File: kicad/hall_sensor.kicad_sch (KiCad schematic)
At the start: 5 parts

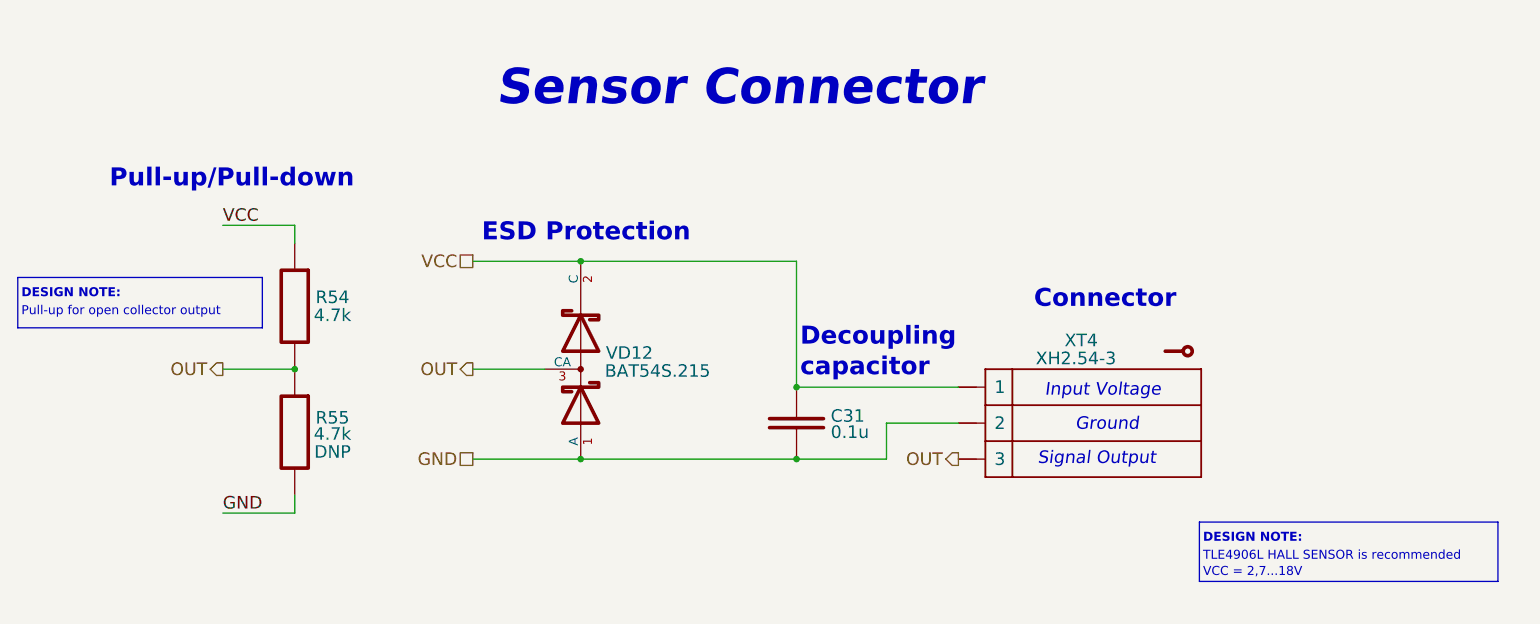
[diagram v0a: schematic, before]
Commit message: Reannotate schematic; Fix 5032 crystal footprint field; Update PCB with 5032 crystal
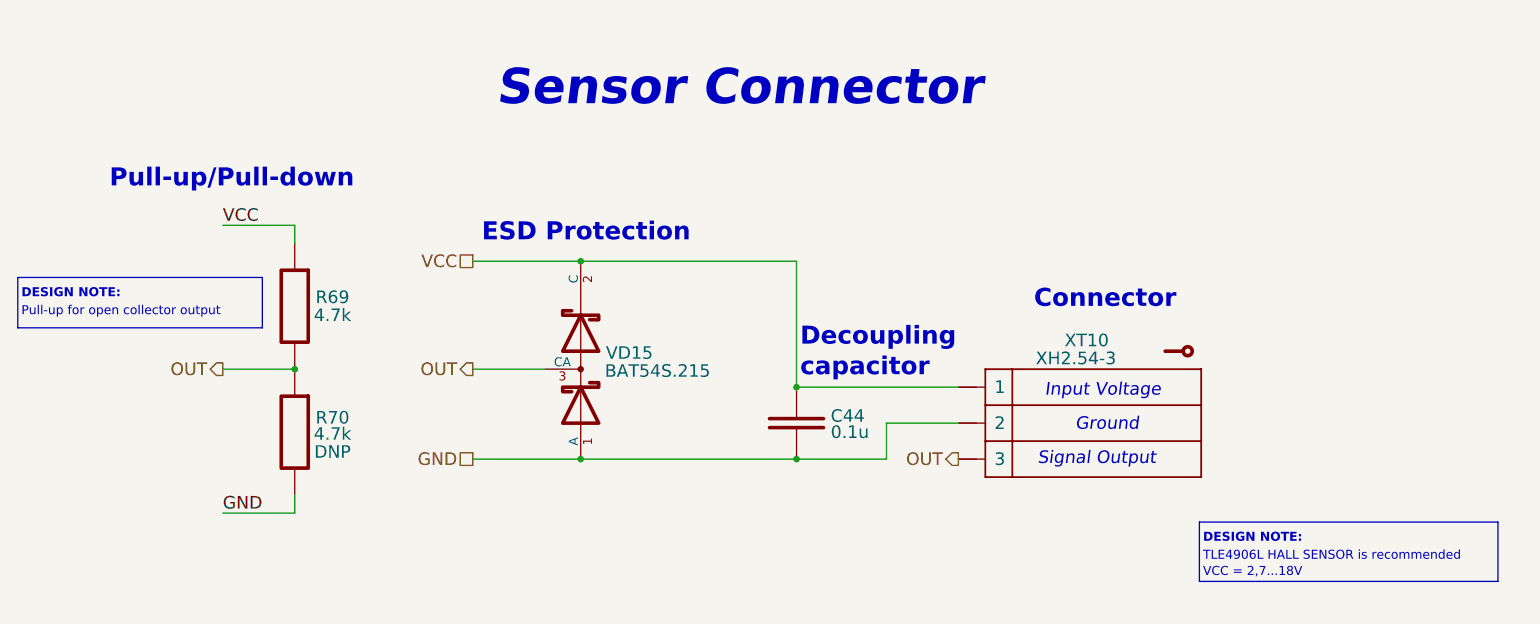
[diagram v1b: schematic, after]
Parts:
- renumbered C31 to C44, R54 to R69, R55 to R70, VD12 to VD15, XT4 to XT10
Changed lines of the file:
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@@
   (symbol (lib_id "Resistors:R_RES") (at 90.424 91.694 270) (unit 1)
     (in_bom yes) (on_board yes)
-    (property "Reference" "R54" (id 0) (at 95.758 90.424 90)
+    (property "Reference" "R69" (id 0) (at 95.758 90.424 90)
       (effects (font (size 1.778 1.778)))
     )
@@
   (symbol (lib_id "Resistors:R_RES") (at 90.424 109.474 270) (unit 1)
     (in_bom yes) (on_board yes)
-    (property "Reference" "R55" (id 0) (at 95.758 107.442 90)
+    (property "Reference" "R70" (id 0) (at 95.758 107.442 90)
       (effects (font (size 1.778 1.778)))
     )
@@
   (symbol (lib_id "Connectors:XT_CONTACT_ARR3") (at 201.93 108.204 0) (unit 1)
     (in_bom yes) (on_board yes)
-    (property "Reference" "XT4" (id 0) (at 199.136 96.52 0)
+    (property "Reference" "XT10" (id 0) (at 199.136 96.52 0)
       (effects (font (size 1.778 1.778)) (justify left))
     )
@@
   (symbol (lib_id "Diodes:VD_SCHOTTKY_PROTECT") (at 130.81 100.584 0) (unit 1)
     (in_bom yes) (on_board yes)
-    (property "Reference" "VD12" (id 0) (at 134.366 98.298 0)
+    (property "Reference" "VD15" (id 0) (at 134.366 98.298 0)
       (effects (font (size 1.778 1.778)) (justify left))
     )
@@
   (symbol (lib_id "Capacitors:C_CAP") (at 161.29 108.204 270) (unit 1)
     (in_bom yes) (on_board yes)
-    (property "Reference" "C31" (id 0) (at 166.116 107.1881 90)
+    (property "Reference" "C44" (id 0) (at 166.116 107.1881 90)
       (effects (font (size 1.778 1.778)) (justify left))
     )

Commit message: Add voltage value to caps, update BOM, SCH, ASM
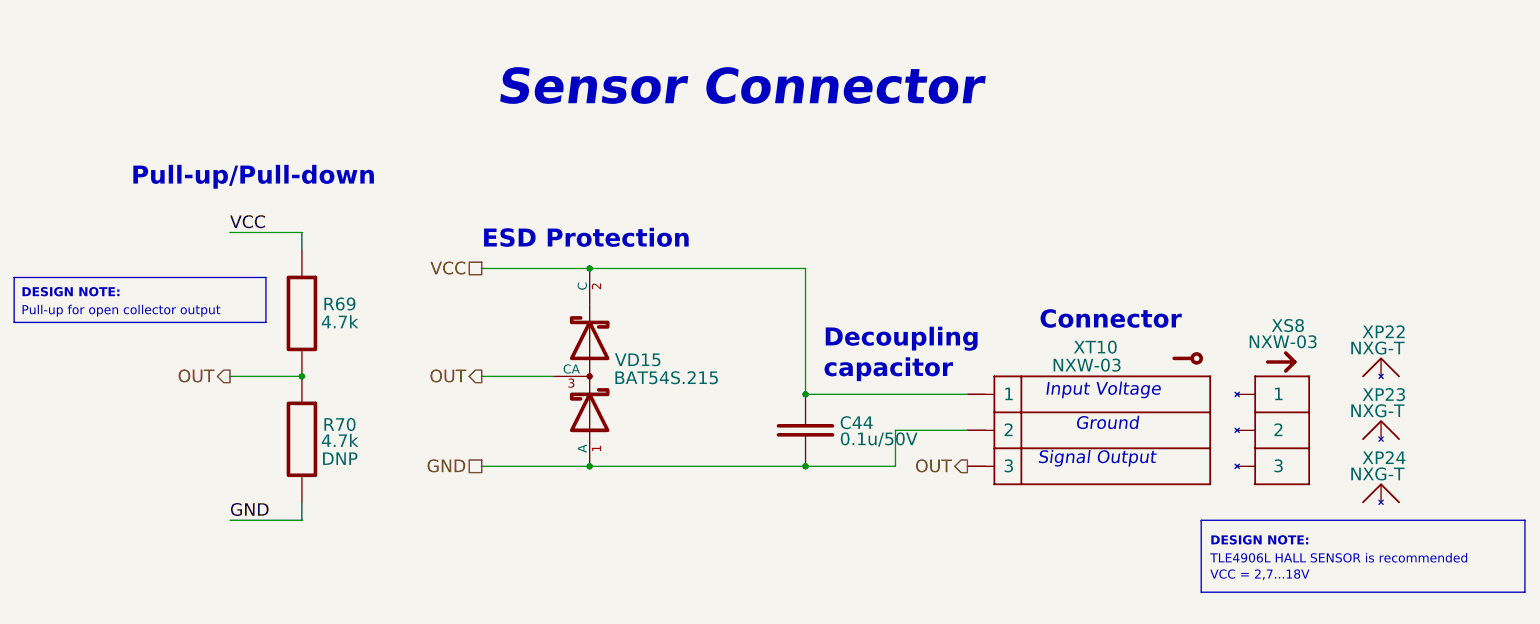
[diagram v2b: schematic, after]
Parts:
- added XP22, XP23, XP24: NXG-T, symbol Connectors:XS_TERMINAL
- added XS8: NXW-03, symbol Connectors:XS_PLUG3
- C44: value 0.1u -> 0.1u/50V; Tolerance (none) -> ±10%; Type (none) -> X7R
- R69, R70: Case/Package 0000 -> 0603; Tolerance ±% -> ±5%
- XT10: value XH2.54-3 -> NXW-03
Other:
- moved on the sheet: C44, R69, R70, VD15, XT10

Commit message: Add docs; Update values of components according to PCB
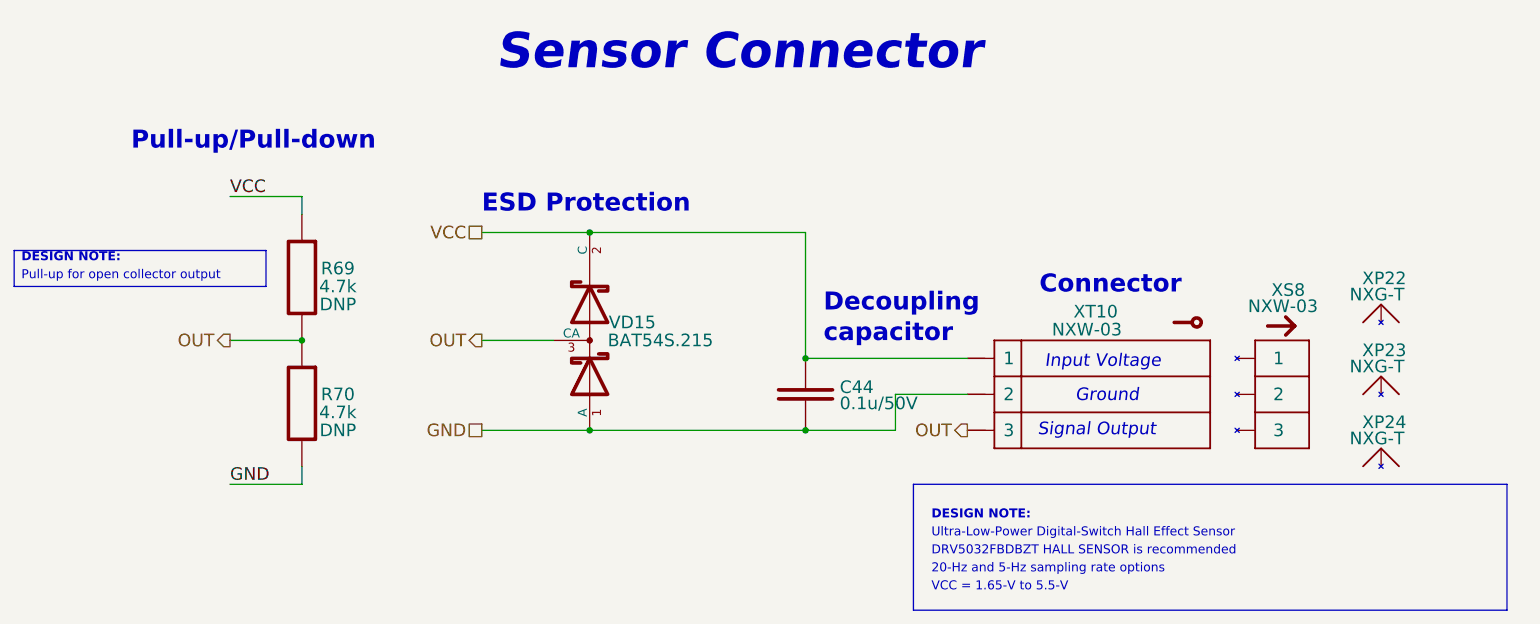
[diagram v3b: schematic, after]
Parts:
- R69: Assembly (none) -> DNP
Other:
- note added: "20-Hz and 5-Hz sampling rate options"
- note added: "DRV5032FBDBZT HALL SENSOR is recommended"
- note added: "Ultra-Low-Power Digital-Switch Hall Effect Sensor"
- note added: "VCC = 1.65-V to 5.5-V"
- note removed: "TLE4906L HALL SENSOR is recommended"
- note removed: "VCC = 2,7...18V"
- moved on the sheet: C44, R69, R70, VD15, XP22, XP23, XP24, XS8, XT10

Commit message: Add wiring diagram; Add work ours (stage 2); refactor folders
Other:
- title: (none) -> RadioSens v1
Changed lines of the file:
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@@
 (kicad_sch (version 20211123) (generator eeschema)
   (paper "A4")
+  (title_block
+    (title "RadioSens v1")
+    (comment 2 "Electrical Circuit")
+  )
   (junction (at 132.08 81.28) (diameter 0) (color 0 0 0 0)
   )
